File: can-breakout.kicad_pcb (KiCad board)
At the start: 2 copper layers, 87 x 50 mm, 34 parts, among them J203 Screw_Terminal_01x02, J301 SEAM-50-02.0-S-08-2-A-K-TR-ND, J302 SEAF-50-05.0-S-08-2-A-K-TR, U201 SN65HVD256, U202 LM7805_TO220, U203 MIC5365-3.3YD5-TR

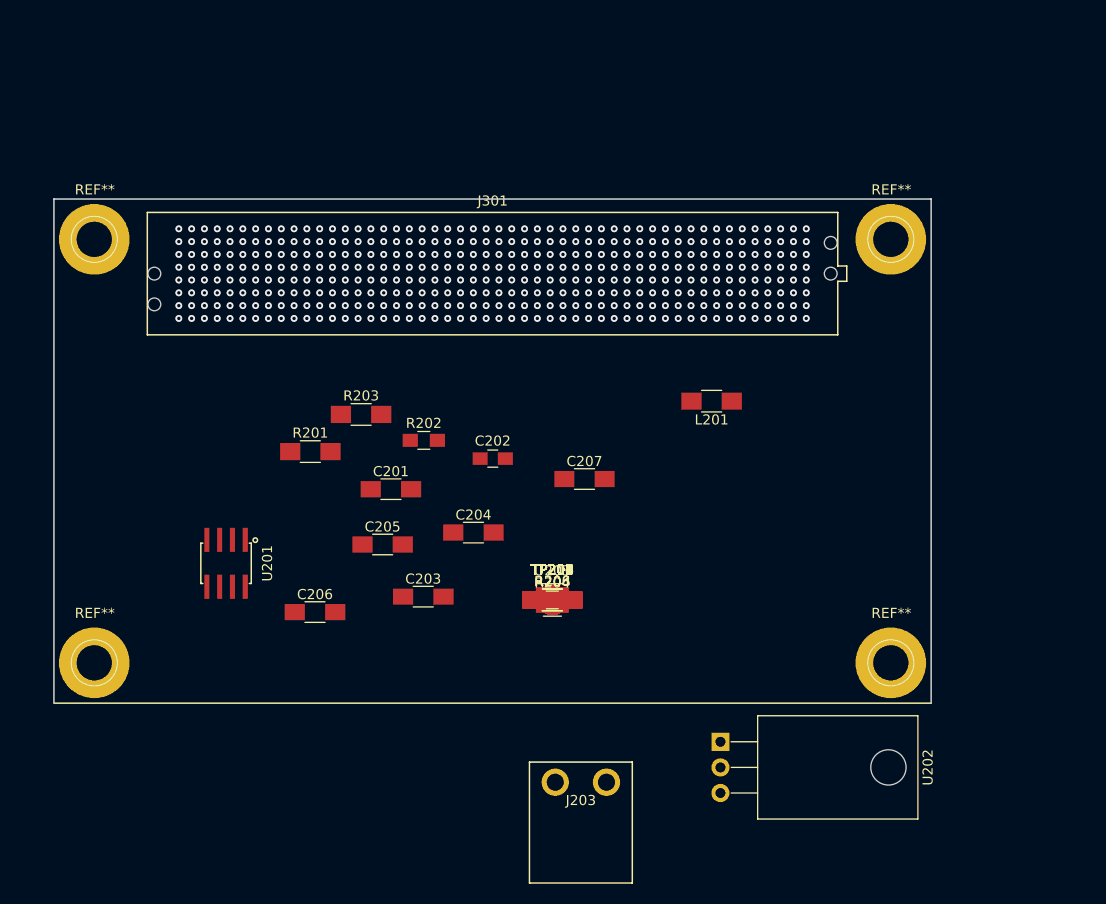
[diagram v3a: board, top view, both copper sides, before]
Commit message: Parts laid out, only routing left
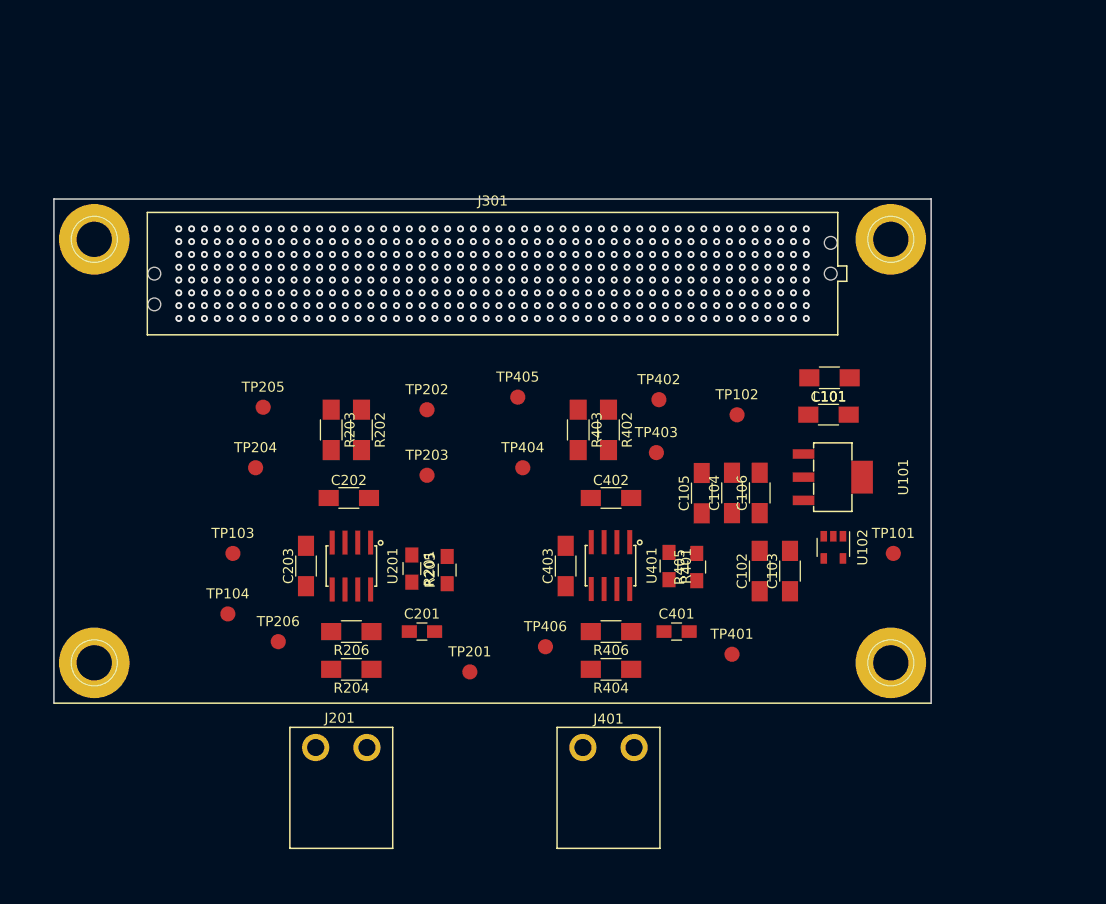
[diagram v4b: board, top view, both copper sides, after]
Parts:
- removed C204, C207: 0u1, Capacitors_SMD:C_1206_HandSoldering
- removed C205, C206: 10u, Capacitors_SMD:C_1206_HandSoldering
- removed J203: Screw_Terminal_01x02, breakout:39532-0002
- removed L201: Ferrite, Resistors_SMD:R_1206_HandSoldering
- removed R208: 4k7, Resistors_SMD:R_1206_HandSoldering
- removed TP207, TP208, TP209, TP210: TEST, Measurement_Points:Measurement_Point_Round-SMD-Pad_Big
- removed U202: LM7805_TO220, TO_SOT_Packages_THT:TO-220-3_Horizontal
- removed U203: MIC5365-3.3YD5-TR, TO_SOT_Packages_SMD:SOT-23-5
- added C101: 10u, Capacitors_SMD:C_1206_HandSoldering, F.Cu at (133.3, 114.0)
- added C102: 10u, Capacitors_SMD:C_1206_HandSoldering, F.Cu at (126.5, 129.5)
- added C103: 0u1, Capacitors_SMD:C_1206_HandSoldering, F.Cu at (129.5, 129.5)
- added C104: 10u, Capacitors_SMD:C_1206_HandSoldering, F.Cu at (123.8, 121.8)
- added C105: 10u, Capacitors_SMD:C_1206_HandSoldering, F.Cu at (120.8, 121.8)
- added C106: 0u1, Capacitors_SMD:C_1206_HandSoldering, F.Cu at (126.5, 121.8)
- added C401: 10n, Capacitors_SMD:C_0805_HandSoldering, F.Cu at (118.2, 135.5)
- added C402: 0u1, Capacitors_SMD:C_1206_HandSoldering, F.Cu at (111.8, 122.2)
- added C403: 0u1, Capacitors_SMD:C_1206_HandSoldering, F.Cu at (107.2, 129.0)
- added J201: Screw_Terminal_01x02, breakout:39532-0002, F.Cu at (85.0, 147.0)
- added J401: Screw_Terminal_01x02, breakout:39532-0002, F.Cu at (111.5, 147.0)
- added L101: Ferrite, Resistors_SMD:R_1206_HandSoldering, F.Cu at (133.4, 110.3)
- added R205: 10k, Resistors_SMD:R_0805_HandSoldering, F.Cu at (95.5, 129.4)
- added R401: DNC, Resistors_SMD:R_0805_HandSoldering, F.Cu at (117.5, 129.0)
- added R402: 4k7, Resistors_SMD:R_1206_HandSoldering, F.Cu at (111.5, 115.5)
- added R403: 4k7, Resistors_SMD:R_1206_HandSoldering, F.Cu at (108.5, 115.5)
- added R404: 60, Resistors_SMD:R_1206_HandSoldering, F.Cu at (111.8, 139.2)
- added R405: 10k, Resistors_SMD:R_0805_HandSoldering, F.Cu at (120.2, 129.1)
- added R406: 60, Resistors_SMD:R_1206_HandSoldering, F.Cu at (111.8, 135.5)
- added TP101: TEST, Measurement_Points:Measurement_Point_Round-SMD-Pad_Small, F.Cu at (139.8, 127.8)
- added TP102: TEST, Measurement_Points:Measurement_Point_Round-SMD-Pad_Small, F.Cu at (124.2, 114.0)
- added TP103: TEST, Measurement_Points:Measurement_Point_Round-SMD-Pad_Small, F.Cu at (74.2, 127.8)
- added TP104: TEST, Measurement_Points:Measurement_Point_Round-SMD-Pad_Small, F.Cu at (73.8, 133.8)
- added TP401: TEST, Measurement_Points:Measurement_Point_Round-SMD-Pad_Small, F.Cu at (123.8, 137.8)
- added TP402: TEST, Measurement_Points:Measurement_Point_Round-SMD-Pad_Small, F.Cu at (116.5, 112.5)
- added TP403: TEST, Measurement_Points:Measurement_Point_Round-SMD-Pad_Small, F.Cu at (116.2, 117.8)
- added TP404: TEST, Measurement_Points:Measurement_Point_Round-SMD-Pad_Small, F.Cu at (103.0, 119.2)
- added TP405: TEST, Measurement_Points:Measurement_Point_Round-SMD-Pad_Small, F.Cu at (102.5, 112.2)
- added TP406: TEST, Measurement_Points:Measurement_Point_Round-SMD-Pad_Small, F.Cu at (105.2, 137.0)
- added U101: UA78M05IDCYR, breakout:TI_SOT-223-4, F.Cu at (133.7, 120.2)
- added U102: MIC5365-3.3YD5-TR, TO_SOT_Packages_SMD:SOT-23-5, F.Cu at (133.8, 127.2)
- added U401: SN65HVD256, breakout:TI_SOIC8, F.Cu at (111.7, 129.0)
- C201: value 10u -> 10n; footprint Capacitors_SMD:C_1206_HandSoldering -> Capacitors_SMD:C_0805_HandSoldering
- C202: value 10n -> 0u1; footprint Capacitors_SMD:C_0805_HandSoldering -> Capacitors_SMD:C_1206_HandSoldering
- C203: value 10u -> 0u1
- R201: value 60 -> DNC; footprint Resistors_SMD:R_1206_HandSoldering -> Resistors_SMD:R_0805_HandSoldering
- R202: value 10k -> 4k7; footprint Resistors_SMD:R_0805_HandSoldering -> Resistors_SMD:R_1206_HandSoldering
- R203: value 60 -> 4k7
- R204: value DNC -> 60; footprint Resistors_SMD:R_0805_HandSoldering -> Resistors_SMD:R_1206_HandSoldering
- R206: value 4k7 -> 60
- TP201, TP202, TP203, TP204, TP205, TP206: footprint Measurement_Points:Measurement_Point_Round-SMD-Pad_Big -> Measurement_Points:Measurement_Point_Round-SMD-Pad_Small
- moved TP205 34.5 mm to (77.2, 113.2)
- moved TP204 32.2 mm to (76.5, 119.2)
- moved TP206 27.5 mm to (78.8, 136.5)
- moved TP202 22.6 mm to (93.5, 113.5)
- moved R204 21.1 mm to (86.0, 139.2), turned to 180 degrees
- moved R206 20.2 mm to (86.0, 135.5), turned to 180 degrees
- moved TP203 17.5 mm to (93.5, 120.0)
- moved R201 15.4 mm to (92.0, 129.2), turned to 270 degrees
- moved C202 14.8 mm to (85.8, 122.2)
- moved C201 14.5 mm to (93.0, 135.5)
- moved U201 12.4 mm to (86.0, 129.0)
- moved C203 12.0 mm to (81.5, 129.0), turned to 90 degrees
- moved TP201 10.9 mm to (97.8, 139.5)
- moved R202 6.27 mm to (87.0, 115.5), turned to 270 degrees
- moved R203 3.34 mm to (84.0, 115.5), turned to 270 degrees
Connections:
- net Net-(J301-PadC18) renamed /CONNECTOR/CAN1_TX
- net Net-(J301-PadD17) renamed /CONNECTOR/CAN1_RX
- C202 pad 1: Net-(C202-Pad1) -> +5V
- J301 pad A1: /CAN_TRANSCEIVER/VBAT -> /CONNECTOR/VSUPPLY
- J301 pad A2: /CAN_TRANSCEIVER/VBAT -> /CONNECTOR/VSUPPLY
- J301 pad A28: GND -> Net-(J301-PadA28)
- J301 pad A37: GND -> Net-(J301-PadA37)
- J301 pad A40: GND -> Net-(J301-PadA40)
- J301 pad A43: GND -> Net-(J301-PadA43)
- J301 pad B1: Net-(J301-PadB1) -> /CONNECTOR/VSUPPLY
- J301 pad B14: GND -> Net-(J301-PadB14)
- J301 pad B2: Net-(J301-PadB2) -> /CONNECTOR/VSUPPLY
- J301 pad B31: GND -> Net-(J301-PadB31)
- J301 pad B38: GND -> Net-(J301-PadB38)
- J301 pad B41: GND -> Net-(J301-PadB41)
- J301 pad B44: GND -> Net-(J301-PadB44)
- J301 pad B47: GND -> Net-(J301-PadB47)
- J301 pad C1: Net-(J301-PadC1) -> /CONNECTOR/VSUPPLY
- J301 pad C2: Net-(J301-PadC2) -> /CONNECTOR/VSUPPLY
- J301 pad C21: GND -> Net-(J301-PadC21)
- J301 pad C24: GND -> Net-(J301-PadC24)
- J301 pad C27: GND -> Net-(J301-PadC27)
- J301 pad C3: GND -> Net-(J301-PadC3)
- J301 pad C30: GND -> Net-(J301-PadC30)
- J301 pad C33: GND -> Net-(J301-PadC33)
- J301 pad C36: GND -> Net-(J301-PadC36)
- J301 pad C39: GND -> Net-(J301-PadC39)
- J301 pad C4: GND -> Net-(J301-PadC3)
- J301 pad C42: GND -> Net-(J301-PadC42)
- J301 pad C45: GND -> Net-(J301-PadC45)
- J301 pad D20: GND -> Net-(J301-PadD20)
- J301 pad D23: GND -> Net-(J301-PadD23)
- J301 pad D26: GND -> Net-(J301-PadD26)
- J301 pad D29: GND -> Net-(J301-PadD29)
- J301 pad D32: GND -> Net-(J301-PadD32)
- J301 pad D35: GND -> Net-(J301-PadD35)
- J301 pad D38: GND -> Net-(J301-PadD38)
- J301 pad D41: GND -> Net-(J301-PadD41)
- J301 pad D44: GND -> Net-(J301-PadD44)
- J301 pad E19: GND -> Net-(J301-PadE19)
- J301 pad E22: GND -> Net-(J301-PadE22)
- J301 pad E25: GND -> Net-(J301-PadE25)
- J301 pad E28: GND -> Net-(J301-PadE28)
- J301 pad E31: GND -> Net-(J301-PadE31)
- J301 pad E34: GND -> Net-(J301-PadE34)
- J301 pad E37: GND -> Net-(J301-PadE37)
- J301 pad E40: GND -> Net-(J301-PadE40)
- J301 pad E43: GND -> Net-(J301-PadE43)
- J301 pad E46: GND -> Net-(J301-PadE46)
- J301 pad F10: GND -> Net-(J301-PadF10)
- J301 pad F15: GND -> Net-(J301-PadF15)
- J301 pad F21: GND -> Net-(J301-PadF21)
- J301 pad F24: GND -> Net-(J301-PadF24)
- J301 pad F27: GND -> Net-(J301-PadF27)
- J301 pad F30: GND -> Net-(J301-PadF30)
- J301 pad F33: GND -> Net-(J301-PadF33)
- J301 pad F36: GND -> Net-(J301-PadF36)
- J301 pad F39: GND -> Net-(J301-PadF39)
- J301 pad F42: GND -> Net-(J301-PadF42)
- J301 pad F45: GND -> Net-(J301-PadF45)
- J301 pad F49: GND -> Net-(J301-PadF49)
- J301 pad G17: GND -> Net-(J301-PadG17)
- J301 pad G20: GND -> Net-(J301-PadG20)
- J301 pad G23: GND -> Net-(J301-PadG23)
- J301 pad G26: GND -> Net-(J301-PadG26)
- J301 pad G29: GND -> Net-(J301-PadG29)
- J301 pad G3: GND -> Net-(J301-PadG3)
- J301 pad G32: GND -> Net-(J301-PadG32)
- J301 pad G35: GND -> Net-(J301-PadG35)
- J301 pad G38: GND -> Net-(J301-PadG38)
- J301 pad G41: GND -> Net-(J301-PadG41)
- J301 pad G44: GND -> Net-(J301-PadG44)
- J301 pad G47: GND -> Net-(J301-PadG47)
- J301 pad G50: GND -> Net-(J301-PadG50)
- J301 pad H19: GND -> Net-(J301-PadH19)
- J301 pad H22: GND -> Net-(J301-PadH22)
- J301 pad H25: GND -> Net-(J301-PadH25)
- J301 pad H28: GND -> Net-(J301-PadH28)
- J301 pad H31: GND -> Net-(J301-PadH31)
- J301 pad H34: GND -> Net-(J301-PadH34)
- J301 pad H37: GND -> Net-(J301-PadH37)
- J301 pad H40: GND -> Net-(J301-PadH40)
- J301 pad H43: GND -> Net-(J301-PadH43)
- J301 pad H46: GND -> Net-(J301-PadH46)
- J301 pad H49: GND -> Net-(J301-PadH49)
- J302 pad A1: /CAN_TRANSCEIVER/VBAT -> /CONNECTOR/VSUPPLY
- J302 pad A2: /CAN_TRANSCEIVER/VBAT -> /CONNECTOR/VSUPPLY
- J302 pad A28: GND -> Net-(J301-PadA28)
- J302 pad A37: GND -> Net-(J301-PadA37)
- J302 pad A40: GND -> Net-(J301-PadA40)
- J302 pad A43: GND -> Net-(J301-PadA43)
- J302 pad B1: Net-(J301-PadB1) -> /CONNECTOR/VSUPPLY
- J302 pad B14: GND -> Net-(J301-PadB14)
- J302 pad B2: Net-(J301-PadB2) -> /CONNECTOR/VSUPPLY
- J302 pad B31: GND -> Net-(J301-PadB31)
- J302 pad B38: GND -> Net-(J301-PadB38)
- J302 pad B41: GND -> Net-(J301-PadB41)
- J302 pad B44: GND -> Net-(J301-PadB44)
- J302 pad B47: GND -> Net-(J301-PadB47)
- J302 pad C1: Net-(J301-PadC1) -> /CONNECTOR/VSUPPLY
- J302 pad C2: Net-(J301-PadC2) -> /CONNECTOR/VSUPPLY
- J302 pad C21: GND -> Net-(J301-PadC21)
- J302 pad C24: GND -> Net-(J301-PadC24)
- J302 pad C27: GND -> Net-(J301-PadC27)
- J302 pad C3: GND -> Net-(J301-PadC3)
- J302 pad C30: GND -> Net-(J301-PadC30)
- J302 pad C33: GND -> Net-(J301-PadC33)
- J302 pad C36: GND -> Net-(J301-PadC36)
- J302 pad C39: GND -> Net-(J301-PadC39)
- J302 pad C4: GND -> Net-(J301-PadC3)
- J302 pad C42: GND -> Net-(J301-PadC42)
- J302 pad C45: GND -> Net-(J301-PadC45)
- J302 pad D20: GND -> Net-(J301-PadD20)
- J302 pad D23: GND -> Net-(J301-PadD23)
- J302 pad D26: GND -> Net-(J301-PadD26)
- J302 pad D29: GND -> Net-(J301-PadD29)
- J302 pad D32: GND -> Net-(J301-PadD32)
- J302 pad D35: GND -> Net-(J301-PadD35)
- J302 pad D38: GND -> Net-(J301-PadD38)
- J302 pad D41: GND -> Net-(J301-PadD41)
- J302 pad D44: GND -> Net-(J301-PadD44)
- J302 pad E19: GND -> Net-(J301-PadE19)
- J302 pad E22: GND -> Net-(J301-PadE22)
- J302 pad E25: GND -> Net-(J301-PadE25)
- J302 pad E28: GND -> Net-(J301-PadE28)
- J302 pad E31: GND -> Net-(J301-PadE31)
- J302 pad E34: GND -> Net-(J301-PadE34)
- J302 pad E37: GND -> Net-(J301-PadE37)
- J302 pad E40: GND -> Net-(J301-PadE40)
- J302 pad E43: GND -> Net-(J301-PadE43)
- J302 pad E46: GND -> Net-(J301-PadE46)
- J302 pad F10: GND -> Net-(J301-PadF10)
- J302 pad F15: GND -> Net-(J301-PadF15)
- J302 pad F21: GND -> Net-(J301-PadF21)
- J302 pad F24: GND -> Net-(J301-PadF24)
- J302 pad F27: GND -> Net-(J301-PadF27)
- J302 pad F30: GND -> Net-(J301-PadF30)
- J302 pad F33: GND -> Net-(J301-PadF33)
- J302 pad F36: GND -> Net-(J301-PadF36)
- J302 pad F39: GND -> Net-(J301-PadF39)
- J302 pad F42: GND -> Net-(J301-PadF42)
- J302 pad F45: GND -> Net-(J301-PadF45)
- J302 pad F49: GND -> Net-(J301-PadF49)
- J302 pad G17: GND -> Net-(J301-PadG17)
- J302 pad G20: GND -> Net-(J301-PadG20)
- J302 pad G23: GND -> Net-(J301-PadG23)
- J302 pad G26: GND -> Net-(J301-PadG26)
- J302 pad G29: GND -> Net-(J301-PadG29)
- J302 pad G3: GND -> Net-(J301-PadG3)
- J302 pad G32: GND -> Net-(J301-PadG32)
- J302 pad G35: GND -> Net-(J301-PadG35)
- J302 pad G38: GND -> Net-(J301-PadG38)
- J302 pad G41: GND -> Net-(J301-PadG41)
- J302 pad G44: GND -> Net-(J301-PadG44)
- J302 pad G47: GND -> Net-(J301-PadG47)
- J302 pad G50: GND -> Net-(J301-PadG50)
- J302 pad H19: GND -> Net-(J301-PadH19)
- J302 pad H22: GND -> Net-(J301-PadH22)
- J302 pad H25: GND -> Net-(J301-PadH25)
- J302 pad H28: GND -> Net-(J301-PadH28)
- J302 pad H31: GND -> Net-(J301-PadH31)
- J302 pad H34: GND -> Net-(J301-PadH34)
- J302 pad H37: GND -> Net-(J301-PadH37)
- J302 pad H40: GND -> Net-(J301-PadH40)
- J302 pad H43: GND -> Net-(J301-PadH43)
- J302 pad H46: GND -> Net-(J301-PadH46)
- J302 pad H49: GND -> Net-(J301-PadH49)
- R201 pad 1: Net-(J203-Pad1) -> +3V3
- R201 pad 2: Net-(C202-Pad1) -> Net-(R201-Pad2)
- R202 pad 1: Net-(R202-Pad1) -> /CONNECTOR/CAN0_TX
- R202 pad 2: GND -> Net-(R202-Pad2)
- R203 pad 1: Net-(C202-Pad1) -> /CONNECTOR/CAN0_RX
- R203 pad 2: Net-(J203-Pad2) -> Net-(R203-Pad2)
- R204 pad 1: +3V3 -> Net-(J201-Pad1)
- R204 pad 2: Net-(R202-Pad1) -> Net-(C201-Pad1)
- R206 pad 1: /CONNECTOR/CAN0_TX -> Net-(C201-Pad1)
- R206 pad 2: Net-(R206-Pad2) -> Net-(J201-Pad2)
- TP201 pad 1: +5V -> Net-(J201-Pad1)
- TP202 pad 1: Net-(C201-Pad1) -> /CONNECTOR/CAN0_TX
- TP203 pad 1: +3V3 -> Net-(R202-Pad2)
- TP204 pad 1: Net-(J203-Pad1) -> Net-(R203-Pad2)
- TP205 pad 1: /CONNECTOR/CAN0_TX -> /CONNECTOR/CAN0_RX
- TP206 pad 1: Net-(R206-Pad2) -> Net-(J201-Pad2)
- U201 pad 1: Net-(R206-Pad2) -> Net-(R202-Pad2)
- U201 pad 4: Net-(R208-Pad2) -> Net-(R203-Pad2)
- U201 pad 6: Net-(J203-Pad2) -> Net-(J201-Pad2)
- U201 pad 7: Net-(J203-Pad1) -> Net-(J201-Pad1)
- U201 pad 8: Net-(R202-Pad1) -> Net-(R201-Pad2)
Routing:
- net Net-(J301-PadH49): vias 0 -> 1
- net Net-(J301-PadH46): vias 0 -> 1
- net Net-(J301-PadH43): vias 0 -> 1
- net Net-(J301-PadH40): vias 0 -> 1
- net Net-(J301-PadH37): vias 0 -> 1
- net Net-(J301-PadH34): vias 0 -> 1
- net Net-(J301-PadH31): vias 0 -> 1
- net Net-(J301-PadH28): vias 0 -> 1
- net Net-(J301-PadH25): vias 0 -> 1
- net Net-(J301-PadH22): vias 0 -> 1
- net Net-(J301-PadH19): vias 0 -> 1
- net Net-(J301-PadG50): vias 0 -> 1
- net Net-(J301-PadG47): vias 0 -> 1
- net Net-(J301-PadG44): vias 0 -> 1
- net Net-(J301-PadG41): vias 0 -> 1
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
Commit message: Finish layout and generate Gerber files
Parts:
- moved TP102 2.94 mm to (126.5, 112.0)
- moved TP101 1.27 mm to (139.2, 126.6)
- moved J401 1.19 mm to (110.3, 146.9)
- moved R401 0.10 mm to (117.5, 129.1)
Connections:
- J301 pad C3: Net-(J301-PadC3) -> GND
- J301 pad C4: Net-(J301-PadC3) -> GND
- J302 pad C3: Net-(J301-PadC3) -> GND
- J302 pad C4: Net-(J301-PadC3) -> GND
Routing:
- net GND: track 0.00 -> 197.6 mm, vias 4 -> 10
- net +5V: track 0.00 -> 77.1 mm, vias 0 -> 3
- net +3V3: track 0.00 -> 70.8 mm
- net /CONNECTOR/CAN0_RX: track 0.00 -> 40.5 mm
- net /CONNECTOR/CAN0_TX: track 0.00 -> 38.4 mm
- net Net-(J201-Pad1): track 0.00 -> 30.8 mm
- net Net-(J401-Pad1): track 0.00 -> 30.1 mm
- net /CONNECTOR/VSUPPLY: track 0.00 -> 23.4 mm
- net /CONNECTOR/CAN1_TX: track 0.00 -> 22.2 mm
- net /CONNECTOR/CAN1_RX: track 0.00 -> 21.6 mm
- net Net-(J201-Pad2): track 0.00 -> 21.0 mm
- net Net-(J401-Pad2): track 0.00 -> 20.4 mm
- net Net-(R202-Pad2): track 0.00 -> 17.6 mm
- net Net-(R203-Pad2): track 0.00 -> 16.7 mm
- net Net-(R403-Pad2): track 0.00 -> 15.9 mm
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- added copper zone on B.Cu, net GND
- added copper zone on F.Cu, net GND
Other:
- board size 87 x 50 mm -> 87 x 59.9 mm
